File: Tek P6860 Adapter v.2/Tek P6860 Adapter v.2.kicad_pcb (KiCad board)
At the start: 2 copper layers, 36.6 x 69.3 mm, 6 parts, among them J1 Conn_01x08, J2 Conn_01x08, J3 Conn_01x02, J4 P6860_Pads, J5 Conn_01x09, SW1 SW_DIP_x09

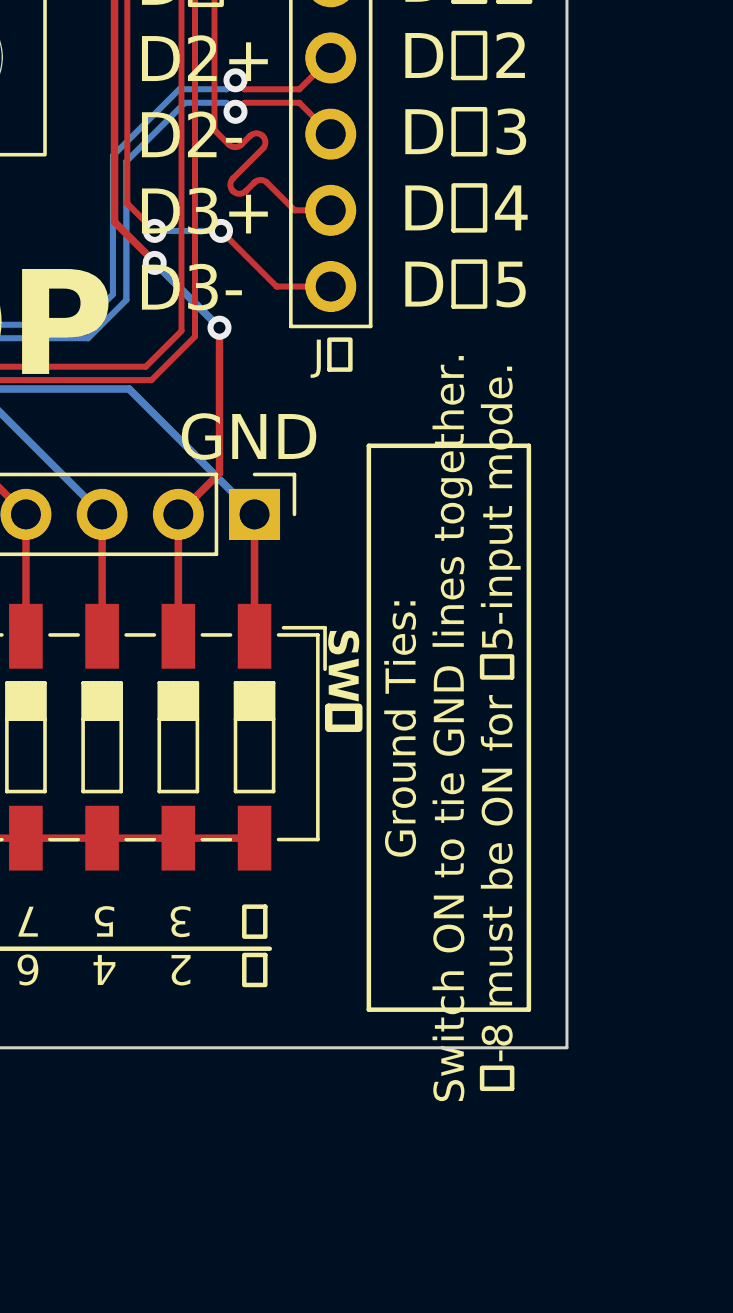
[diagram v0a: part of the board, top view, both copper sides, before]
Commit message: Add files via upload
silkscreen fix
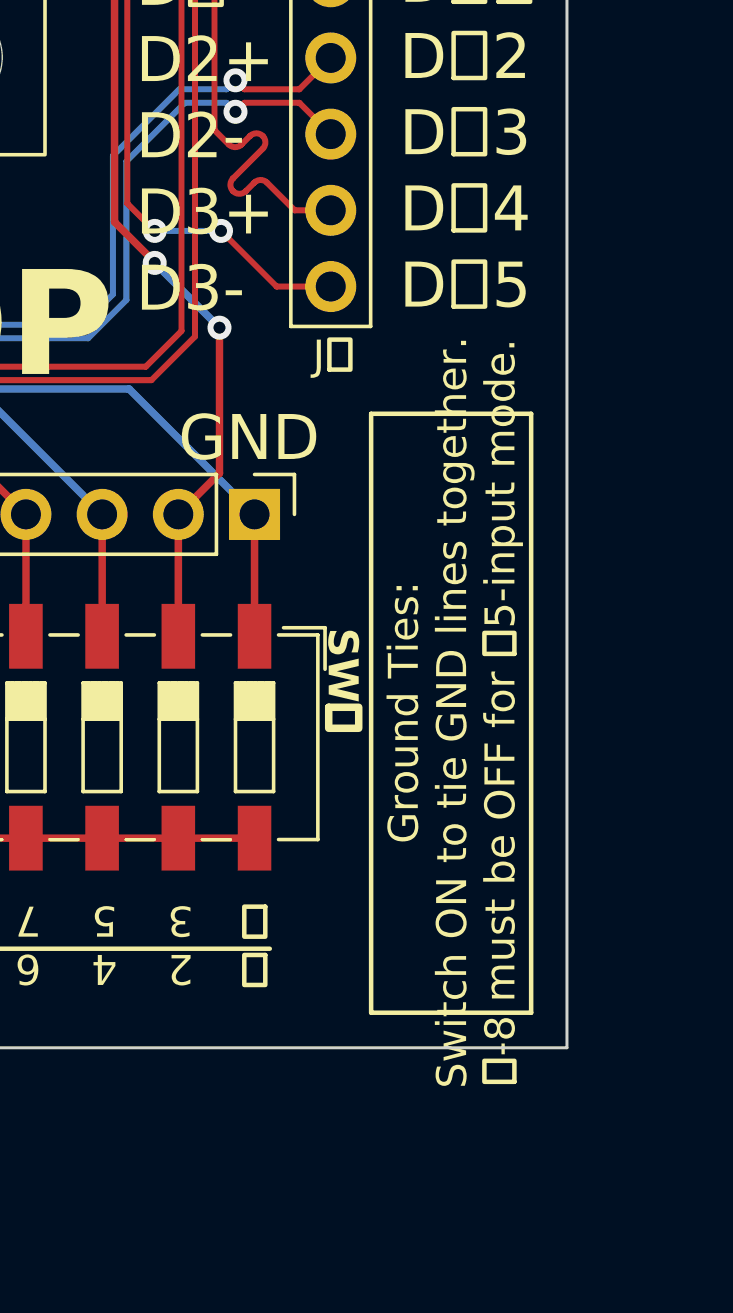
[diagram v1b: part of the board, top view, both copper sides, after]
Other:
- board text added: "Ground Ties: Switch ON to tie GND lines together. -8 must be OFF for 5-input mode."
- board text removed: "Ground Ties: Switch ON to tie GND lines together. -8 must be ON for 5-input mode."

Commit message: Add files via upload
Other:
- board text added: "Ground Ties: Switch ON to tie GND lines together. -8 must be OFF for 6-input mode."
- board text added: "6 Inputs"
- board text removed: "Ground Ties: Switch ON to tie GND lines together. -8 must be OFF for 5-input mode."
- board text removed: "5 Inputs"
